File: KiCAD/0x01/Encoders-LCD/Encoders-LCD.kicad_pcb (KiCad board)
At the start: 2 copper layers, 110 x 76 mm, 35 parts, among them J1 Conn_B1, J2 Conn_B4, J3 Conn_B3, SW1 RotaryEncoder_Switch, SW2 RotaryEncoder_Switch, SW3 RotaryEncoder_Switch, SW4 SW_Push_LED, U1 ST7789, U2 CD74HC4067M, U3 ST7789

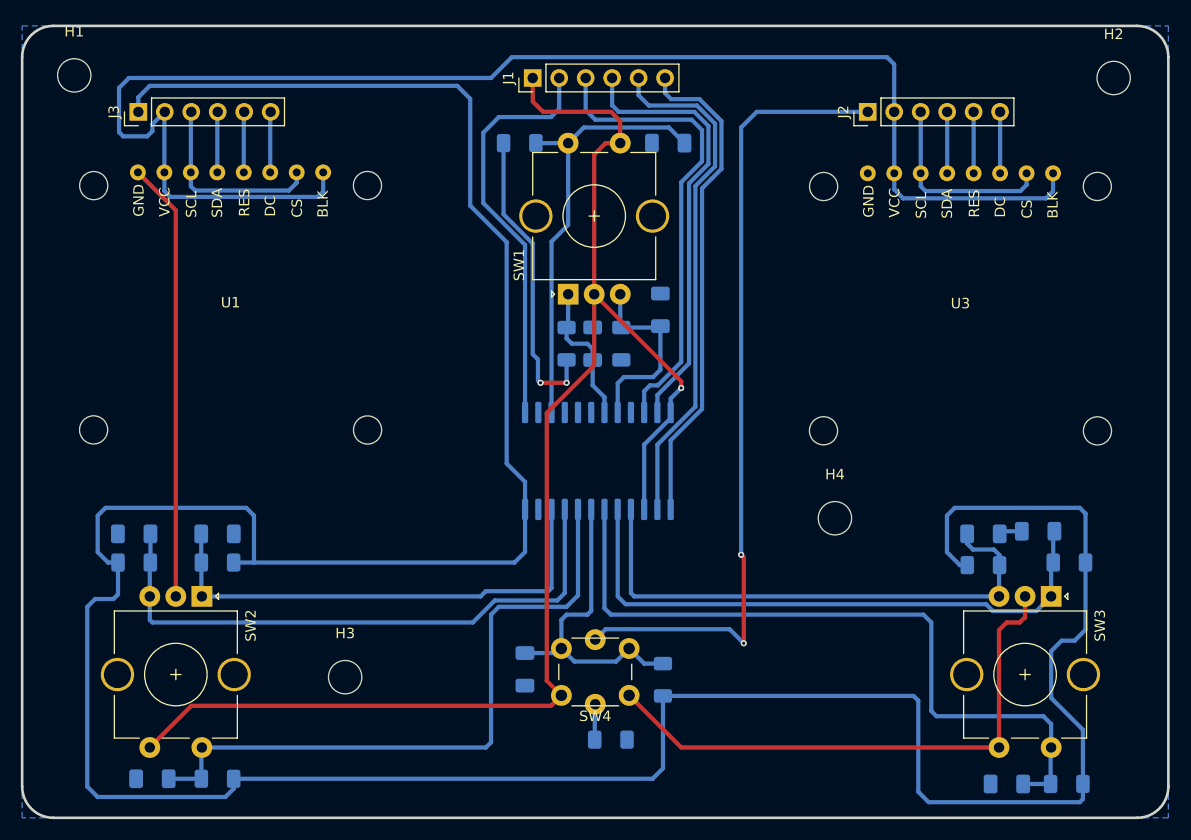
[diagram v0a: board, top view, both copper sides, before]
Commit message: fix lcd encoders
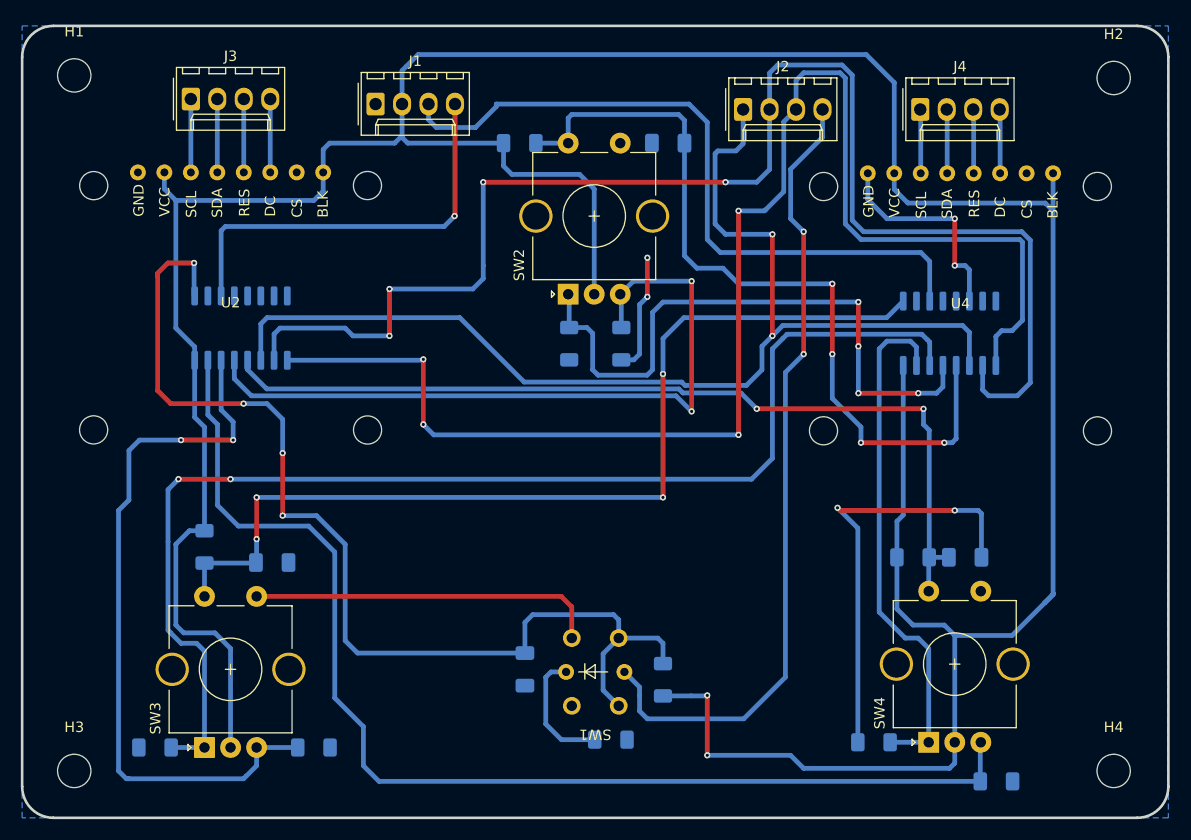
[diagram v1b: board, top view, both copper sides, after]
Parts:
- removed the C1 at (106.8, 68.8)
- removed the C2 at (56.2, 90.2)
- removed C5, C6, C8, C9: 1uF, Capacitor_SMD:C_1206_3216Metric_Pad1.33x1.80mm_HandSolder
- removed the R8 at (64.2, 113.8)
- removed the R9 at (145.8, 114.2)
- removed the SW2 at (62.8, 96.2)
- removed the U2 at (100.8, 83.2)
- added J4: DISPLAY_R, Connector_Molex:Molex_KK-254_AE-6410-04A_1x04_P2.54mm_Vertical, F.Cu at (131.7, 49.5)
- added R10: 10K, PCM_Resistor_SMD_AKL:R_1206_3216Metric_Pad1.30x1.75mm_HandSolder, B.Cu at (63.0, 91.5)
- added R11: 10K, PCM_Resistor_SMD_AKL:R_1206_3216Metric_Pad1.30x1.75mm_HandSolder, B.Cu at (131.0, 92.5)
- added SW4: RotaryEncoder_Switch, Rotary_Encoder:RotaryEncoder_Alps_EC11E-Switch_Vertical_H20mm_CircularMountingHoles, F.Cu at (132.5, 110.2)
- added U1: 74HC4051, Package_SO:SOP-16_4.4x10.4mm_P1.27mm, B.Cu at (134.5, 71.0)
- added U3: 74HC4051, Package_SO:SOP-16_4.4x10.4mm_P1.27mm, B.Cu at (66.5, 70.5)
- J1: value Conn_B1 -> SIGNALS; footprint Connector_PinHeader_2.54mm:PinHeader_1x06_P2.54mm_Vertical -> Connector_Molex:Molex_KK-254_AE-6410-04A_1x04_P2.54mm_Vertical
- J2: value Conn_B4 -> S_PINS; footprint Connector_PinHeader_2.54mm:PinHeader_1x06_P2.54mm_Vertical -> Connector_Molex:Molex_KK-254_AE-6410-04A_1x04_P2.54mm_Vertical
- J3: value Conn_B3 -> DISPLAY_L; footprint Connector_PinHeader_2.54mm:PinHeader_1x06_P2.54mm_Vertical -> Connector_Molex:Molex_KK-254_AE-6410-04A_1x04_P2.54mm_Vertical
- R7: renamed from R10; value 220 -> 100
- SW1: renamed from SW4; footprint led-switch:SW_PUSH_6mm_LED -> led-sw:led switch
- moved SW3 82.5 mm to (63.0, 110.8), turned to 90 degrees
- moved R3 81.4 mm to (58.2, 110.8)
- moved C3 68.3 mm to (69.5, 93.0)
- moved R5 65.3 mm to (127.2, 110.2), turned to 0 degrees
- moved R2 51.2 mm to (103.0, 72.0), turned to 90 degrees
- moved R4 45.7 mm to (73.5, 110.8), turned to 180 degrees
- moved C4 41.2 mm to (136.0, 92.5), turned to 0 degrees
- moved H4 36.1 mm to (150.2, 113.0)
- moved H3 27.5 mm to (50.5, 113.0)
- moved R6 22.1 mm to (139.0, 114.0)
- moved J1 15.3 mm to (79.4, 49.0), turned to 0 degrees
- moved J2 12.0 mm to (114.7, 49.5), turned to 0 degrees
- moved J3 5.19 mm to (61.7, 48.5), turned to 0 degrees
- moved R1 5.00 mm to (98.0, 72.0)
- renumbered C10 to C1, C7 to C2, R11 to R8, R7 to R9, SW1 to SW2, U1 to U2, U3 to U4
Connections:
- net ROT-1SW renamed /ROT-1SW
- net SFTSW renamed /SFTSW
- C3 pad 1: ROT-3B -> /ROT-2SW
- C4 pad 1: ROT-1A -> /ROT-3SW
- J1 pad 2: MPLEX-B -> VCC
- J1 pad 3: MPLEX-S0 -> /SIG_A
- J1 pad 4: MPLEX-S1 -> /SIG_B
- J2 pad 1: SF-LED -> /S0
- J2 pad 2: 3V3 -> /S1
- J2 pad 3: SPI1_SCK -> /S2
- J2 pad 4: SPI1_TX -> /SF-LED
- J3 pad 1: +5V -> /SPI0_SCK
- J3 pad 2: 3V3 -> /SPI0_TX
- J3 pad 3: SPI0_SCK -> /SPI0_RX
- J3 pad 4: SPI0_TX -> /SPI0_CS
- R1 pad 1: +5V -> GND
- R1 pad 2: ROT-1B -> /ROT-1A
- R2 pad 1: +5V -> GND
- R2 pad 2: ROT-2B -> /ROT-1B
- R3 pad 1: +5V -> GND
- R3 pad 2: ROT-3B -> /ROT-2A
- R4 pad 1: +5V -> GND
- R4 pad 2: ROT-1A -> /ROT-2B
- R5 pad 1: +5V -> GND
- R5 pad 2: ROT-2A -> /ROT-3A
- R6 pad 1: +5V -> GND
- R6 pad 2: ROT-3A -> /ROT-3B
- R8 pad 1: +5V -> VCC
- R9 pad 1: +5V -> VCC
- SW1 pad 4: SF-LED -> /SF-LED
- SW2 pad A: ROT-1A -> /ROT-1A
- SW2 pad B: ROT-1B -> /ROT-1B
- SW2 pad C: GND -> VCC
- SW3 pad A: ROT-3A -> /ROT-2A
- SW3 pad B: ROT-3B -> /ROT-2B
- SW3 pad C: GND -> VCC
- SW3 pad S2: ROT-3SW -> /ROT-2SW
- U2 pad 2: 3V3 -> VCC
- U2 pad 3: SPI0_SCK -> /SPI0_SCK
- U2 pad 4: SPI0_TX -> /SPI0_TX
- U2 pad 5: SPI0_RX -> /SPI0_RX
- U2 pad 6: SPI0_CS -> /SPI0_CS
- U2 pad 7: SPI0_SCK -> /SPI0_SCK
- U2 pad 8: 3V3 -> VCC
- U4 pad 2: 3V3 -> VCC
- U4 pad 3: SPI1_SCK -> /SPI1_SCK
- U4 pad 4: SPI1_TX -> /SPI1_TX
- U4 pad 5: SPI1_RX -> /SPI1_RX
- U4 pad 6: SPI1_CS -> /SPI1_CS
- U4 pad 7: SPI1_SCK -> /SPI1_SCK
- U4 pad 8: 3V3 -> VCC
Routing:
- net +5V: track 351.8 -> 0.00 mm, vias 2 -> 0
- net VCC: track 0.00 -> 332.6 mm, vias 0 -> 2
- net 3V3: track 140.8 -> 0.00 mm
- net /S2: track 0.00 -> 138.2 mm, vias 0 -> 4
- net /S1: track 0.00 -> 136.4 mm, vias 0 -> 4
- net GND: track 236.4 -> 107.4 mm, vias 1 -> 6
- net /ROT-2A: track 0.00 -> 118.9 mm, vias 0 -> 2
- net /ROT-3B: track 0.00 -> 112.6 mm
- net /S0: track 0.00 -> 110.4 mm, vias 0 -> 2
- net /ROT-2SW: track 0.00 -> 93.2 mm, vias 0 -> 4
- net /ROT-3SW: track 0.00 -> 87.0 mm, vias 0 -> 2
- net SF-LED: track 77.6 -> 0.00 mm, vias 2 -> 0
- net /SF-LED: track 0.00 -> 77.3 mm, vias 0 -> 2
- net /SFTSW: track 30.8 -> 103.2 mm, vias 0 -> 4
- net ROT-3SW: track 70.3 -> 0.00 mm
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
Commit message: encoders
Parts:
- removed J4: DISPLAY_R, Connector_Molex:Molex_KK-254_AE-6410-04A_1x04_P2.54mm_Vertical
- removed U3: 74HC4051, Package_SO:SOP-16_4.4x10.4mm_P1.27mm
- removed U4: ST7789, Display-oled:1.14 7789
- J1: value SIGNALS -> Conn_01x03; footprint Connector_Molex:Molex_KK-254_AE-6410-04A_1x04_P2.54mm_Vertical -> Connector_Molex:Molex_KK-254_AE-6410-03A_1x03_P2.54mm_Vertical
- J2: value S_PINS -> MUX_A; footprint Connector_Molex:Molex_KK-254_AE-6410-04A_1x04_P2.54mm_Vertical -> Connector_Molex:Molex_KK-254_AE-6410-06A_1x06_P2.54mm_Vertical
- J3: value DISPLAY_L -> MUX_B; footprint Connector_Molex:Molex_KK-254_AE-6410-04A_1x04_P2.54mm_Vertical -> Connector_Molex:Molex_KK-254_AE-6410-06A_1x06_P2.54mm_Vertical
- U2: value ST7789 -> 74HC4051; footprint Display-oled:1.14 7789 -> Package_SO:SOP-16_4.4x10.4mm_P1.27mm; moved to B.Cu
- moved J1 72.2 mm to (115.5, 111.5), turned to 180 degrees
- moved J2 24.7 mm to (138.5, 56.0), turned to 180 degrees
- moved J3 16.1 mm to (76.0, 56.0), turned to 180 degrees
- moved U1 5.32 mm to (131.0, 67.0), turned to 90 degrees
- moved U2 3.38 mm to (68.5, 67.0), turned to 90 degrees
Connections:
- J1 pad 3: /SIG_A -> /SF-LED
- J2 pad 1: /S0 -> GND
- J2 pad 2: /S1 -> VCC
- J2 pad 3: /S2 -> /SIG_A
- J2 pad 4: /SF-LED -> /S0A
- J3 pad 1: /SPI0_SCK -> GND
- J3 pad 2: /SPI0_TX -> VCC
- J3 pad 3: /SPI0_RX -> /SIG_B
- J3 pad 4: /SPI0_CS -> /S0B
- U1 pad 10: /S1 -> /S1A
- U1 pad 11: /S0 -> /S0A
- U1 pad 9: /S2 -> /S2A
- U2 pad 1: GND -> /SFTSW
- U2 pad 2: VCC -> unconnected-(U2-A6-Pad2)
- U2 pad 3: /SPI0_SCK -> /SIG_B
- U2 pad 4: /SPI0_TX -> unconnected-(U2-A7-Pad4)
- U2 pad 5: /SPI0_RX -> unconnected-(U2-A5-Pad5)
- U2 pad 6: /SPI0_CS -> GND
- U2 pad 7: /SPI0_SCK -> GND
- U2 pad 8: VCC -> GND
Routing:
- net VCC: track 332.6 -> 0.00 mm, vias 2 -> 0
- net /S2: track 138.2 -> 0.00 mm, vias 4 -> 0
- net /S1: track 136.4 -> 0.00 mm, vias 4 -> 0
- net /ROT-2A: track 118.9 -> 0.00 mm, vias 2 -> 0
- net /ROT-3B: track 112.6 -> 0.00 mm
- net /S0: track 110.4 -> 0.00 mm, vias 2 -> 0
- net GND: track 107.4 -> 0.00 mm, vias 6 -> 0
- net /SFTSW: track 103.2 -> 0.00 mm, vias 4 -> 0
- net /ROT-2SW: track 93.2 -> 0.00 mm, vias 4 -> 0
- net /ROT-3SW: track 87.0 -> 0.00 mm, vias 2 -> 0
- net /ROT-1SW: track 78.1 -> 0.00 mm, vias 4 -> 0
- net /SF-LED: track 77.3 -> 0.00 mm, vias 2 -> 0
- net /ROT-1B: track 70.1 -> 0.00 mm, vias 2 -> 0
- net /ROT-2B: track 69.6 -> 0.00 mm, vias 2 -> 0
- net /SIG_A: track 67.6 -> 0.00 mm
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
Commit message: nc programs
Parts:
- moved J2 62.5 mm to (76.0, 56.0)
- moved J3 62.5 mm to (138.5, 56.0)
- moved U1 62.5 mm to (68.5, 67.0)
- moved U2 62.5 mm to (131.0, 67.0)
- moved C4 1.50 mm to (137.5, 92.5)
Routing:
- net VCC: track 0.00 -> 335.3 mm, vias 0 -> 2
- net /ROT-2B: track 0.00 -> 109.1 mm, vias 0 -> 2
- net /ROT-3A: track 0.00 -> 99.4 mm
- net /SFTSW: track 0.00 -> 88.0 mm, vias 0 -> 4
- net GND: track 0.00 -> 68.7 mm, vias 0 -> 4
- net /ROT-3B: track 0.00 -> 68.7 mm
- net /ROT-2A: track 0.00 -> 61.8 mm
- net /ROT-1SW: track 0.00 -> 60.5 mm
- net /ROT-3SW: track 0.00 -> 48.1 mm
- net /SIG_A: track 0.00 -> 47.4 mm, vias 0 -> 4
- net /ROT-1B: track 0.00 -> 40.5 mm, vias 0 -> 2
- net /ROT-1A: track 0.00 -> 39.7 mm, vias 0 -> 2
- net /SIG_B: track 0.00 -> 36.8 mm, vias 0 -> 2
- net /ROT-2SW: track 0.00 -> 34.3 mm
- net /SF-LED: track 0.00 -> 14.4 mm
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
